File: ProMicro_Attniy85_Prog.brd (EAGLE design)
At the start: 31.7 x 21.6 mm, 10 parts, among them U1 ATTINY85-20P

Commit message: Add files via upload
Minor changes
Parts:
- moved R1 1.59 mm to (27.6, 8.89)
- moved R2 1.59 mm to (27.6, 11.4)
- moved R3 1.59 mm to (27.6, 14.0)
- moved LED3 1.31 mm to (23.2, 9.21)
- moved LED1 1.27 mm to (23.2, 14.0)
- moved LED2 1.27 mm to (23.2, 11.4)
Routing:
- net PIN9: track 32.5 -> 30.2 mm
- net PIN7: track 36.5 -> 37.2 mm
- net VCC: track 14.6 -> 14.0 mm

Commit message: Add files via upload
Minor changes
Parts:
- moved C1 0.95 mm to (17.5, 11.4)
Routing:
- net RST: track 11.7 -> 12.7 mm
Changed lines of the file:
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@@
 <wire x1="21.2725" y1="14.9225" x2="21.2725" y2="7.9375" width="0.2032" layer="21"/>
 <wire x1="21.2725" y1="7.9375" x2="24.765" y2="7.9375" width="0.2032" layer="21"/>
-<text x="17.145" y="9.525" size="0.8128" layer="21" rot="R90">10nF</text>
+<text x="16.1925" y="9.525" size="0.8128" layer="21" rot="R90">10nF</text>
 <text x="20.955" y="11.43" size="0.8128" layer="21" rot="R90" align="bottom-center">LED</text>
 <text x="29.845" y="7.62" size="0.8128" layer="21" align="top-right">220ohm</text>
@@
 <elements>
 <element name="U1" library="_hhn_attiny25_45_85 (1)" package="PDIP08_300MIL" value="ATTINY85-20P" x="8.89" y="11.43" smashed="yes" rot="R180"/>
-<element name="C1" library="rc-master-smd" package="C0805" value="" x="18.415" y="11.43" smashed="yes" rot="R270">
-<attribute name="NAME" x="19.685" y="13.208" size="0.8128" layer="25" ratio="18" rot="R270"/>
-<attribute name="VALUE" x="16.637" y="13.208" size="0.6096" layer="27" ratio="10" rot="R270"/>
+<element name="C1" library="rc-master-smd" package="C0805" value="" x="17.4625" y="11.43" smashed="yes" rot="R270">
+<attribute name="NAME" x="16.3195" y="13.6525" size="0.8128" layer="25" ratio="18"/>
+<attribute name="VALUE" x="15.6845" y="13.208" size="0.6096" layer="27" ratio="10" rot="R270"/>
 </element>
 <element name="JP2" library="pinhead" library_urn="urn:adsk.eagle:library:325" package="2X12" package3d_urn="urn:adsk.eagle:package:22420/2" value="" x="16.51" y="19.05" smashed="yes" rot="R180">
@@
 <wire x1="22.86" y1="20.32" x2="22.86" y2="17.78" width="0.4064" layer="1"/>
 <wire x1="25.4" y1="20.32" x2="25.4" y2="17.78" width="0.4064" layer="1"/>
-<wire x1="22.86" y1="17.78" x2="22.5425" y2="17.78" width="0.4064" layer="1"/>
-<wire x1="22.5425" y1="17.78" x2="18.415" y2="13.6525" width="0.4064" layer="1"/>
-<wire x1="18.415" y1="13.6525" x2="18.415" y2="13.716" width="0.4064" layer="1"/>
-<wire x1="18.415" y1="12.446" x2="18.415" y2="13.6525" width="0.4064" layer="1"/>
+<wire x1="17.4625" y1="12.446" x2="17.4625" y2="12.7635" width="0.4064" layer="1"/>
 <wire x1="5.08" y1="15.24" x2="7.874" y2="12.446" width="0.4064" layer="1"/>
-<wire x1="7.874" y1="12.446" x2="18.415" y2="12.446" width="0.4064" layer="1"/>
+<wire x1="7.874" y1="12.446" x2="17.4625" y2="12.446" width="0.4064" layer="1"/>
 <wire x1="22.86" y1="20.32" x2="25.4" y2="20.32" width="0.4064" layer="1"/>
 <via x="16.51" y="6.985" extent="1-16" drill="0.35"/>
@@
 <vertex x="0.3175" y="-0.635"/>
 </polygon>
+<wire x1="17.4625" y1="12.446" x2="22.7965" y2="17.78" width="0.4064" layer="1"/>
+<wire x1="22.7965" y1="17.78" x2="22.86" y2="17.78" width="0.4064" layer="1"/>
+<wire x1="22.86" y1="17.78" x2="22.1275" y2="13.97" width="0" layer="19" extent="1-1"/>
+<wire x1="16.51" y1="6.985" x2="17.4625" y2="12.446" width="0" layer="19" extent="1-1"/>
 </signal>
 <signal name="VCC">
@@
 <wire x1="23.8125" y1="6.6675" x2="22.225" y2="6.6675" width="0.2032" layer="1"/>
 <wire x1="22.225" y1="6.6675" x2="18.4785" y2="10.414" width="0.2032" layer="1"/>
-<wire x1="18.415" y1="10.414" x2="18.4785" y2="10.414" width="0.2032" layer="1"/>
+<wire x1="17.4625" y1="10.414" x2="18.4785" y2="10.414" width="0.2032" layer="1"/>
 <contactref element="JP3" pad="19"/>
 <contactref element="JP3" pad="20"/>

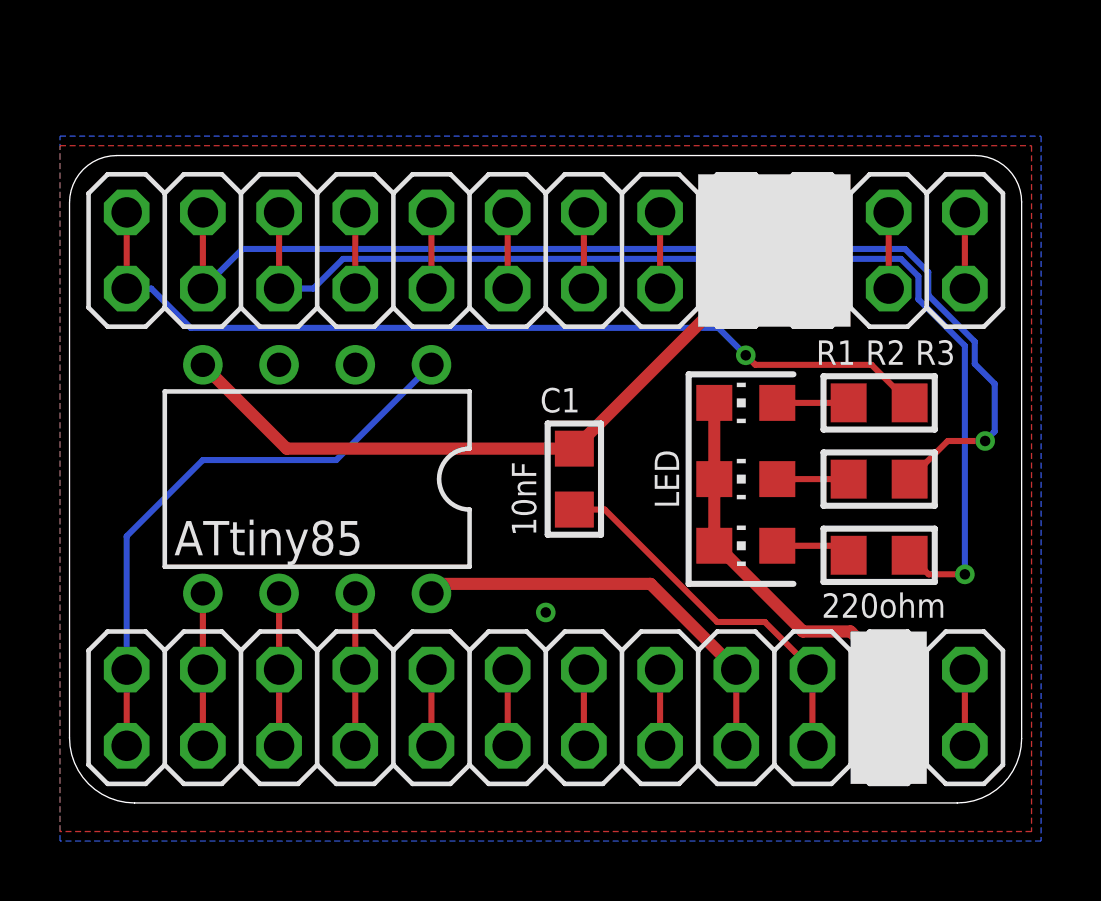
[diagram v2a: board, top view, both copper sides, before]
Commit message: Add files via upload
Wrong size, corrected... the old one only fits on the original pro micro with micro USB
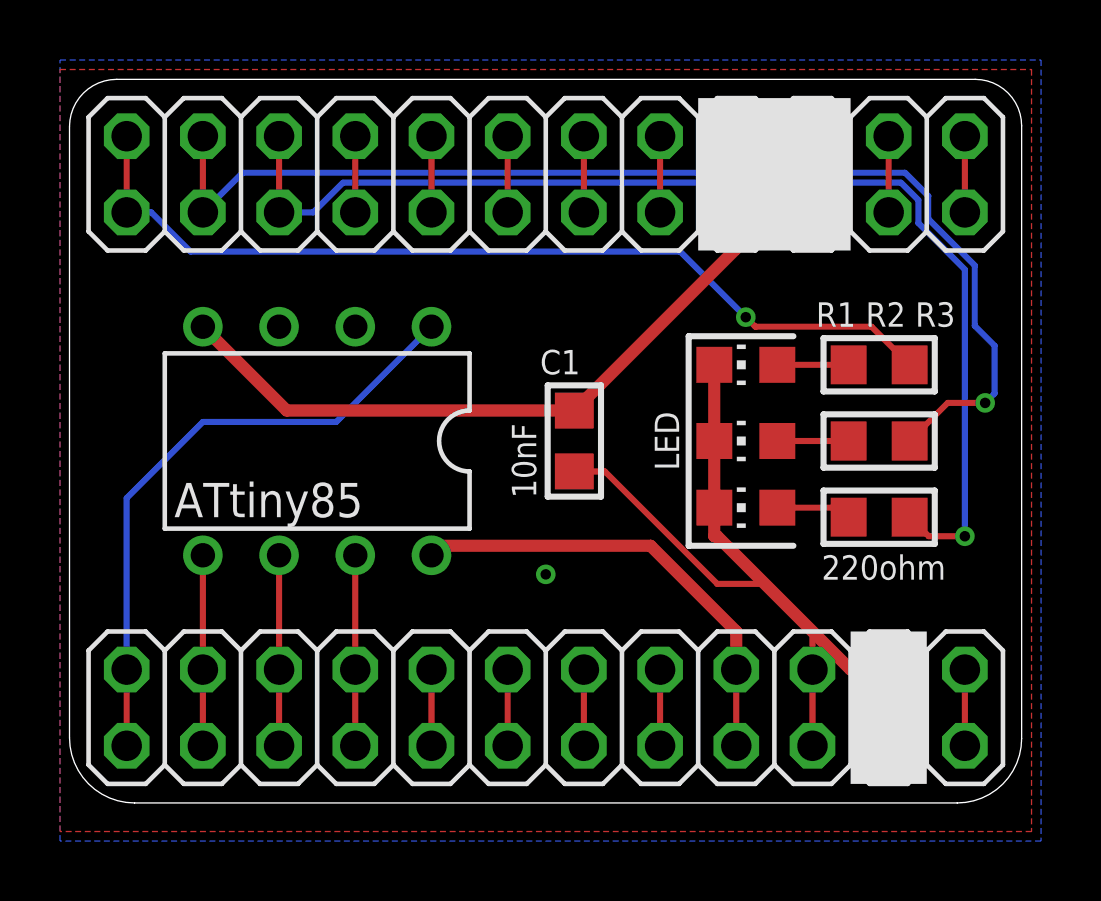
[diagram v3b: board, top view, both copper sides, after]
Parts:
- moved JP2 2.54 mm to (16.5, 21.6)
- moved C1 1.27 mm to (17.5, 12.7)
- moved LED1 1.27 mm to (23.2, 15.2)
- moved LED2 1.27 mm to (23.2, 12.7)
- moved LED3 1.27 mm to (23.2, 10.5)
- moved R1 1.27 mm to (27.6, 10.2)
- moved R2 1.27 mm to (27.6, 12.7)
- moved R3 1.27 mm to (27.6, 15.2)
- moved U1 1.27 mm to (8.89, 12.7)
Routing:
- net GND: track 43.9 -> 46.2 mm
- net PIN8: track 37.3 -> 38.6 mm
- net SCK: track 5.08 -> 6.35 mm
- net MOSI: track 5.08 -> 6.35 mm
- net MISO: track 5.08 -> 6.35 mm
- net VCC: track 14.0 -> 15.3 mm
- net RST: track 12.7 -> 14.0 mm
- net PIN7: track 37.2 -> 38.5 mm
- net PIN10: track 19.5 -> 20.8 mm
- net PIN9: track 30.2 -> 30.7 mm
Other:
- board size 31.7 x 21.6 mm -> 31.7 x 24.1 mm

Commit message: Add files via upload
As a recommendation from the AttinyCore85 Documentation, I've exchanged the capacitor (that was low) to an tantalum polar 100uf, and added another one of 0.1uf as coupler.
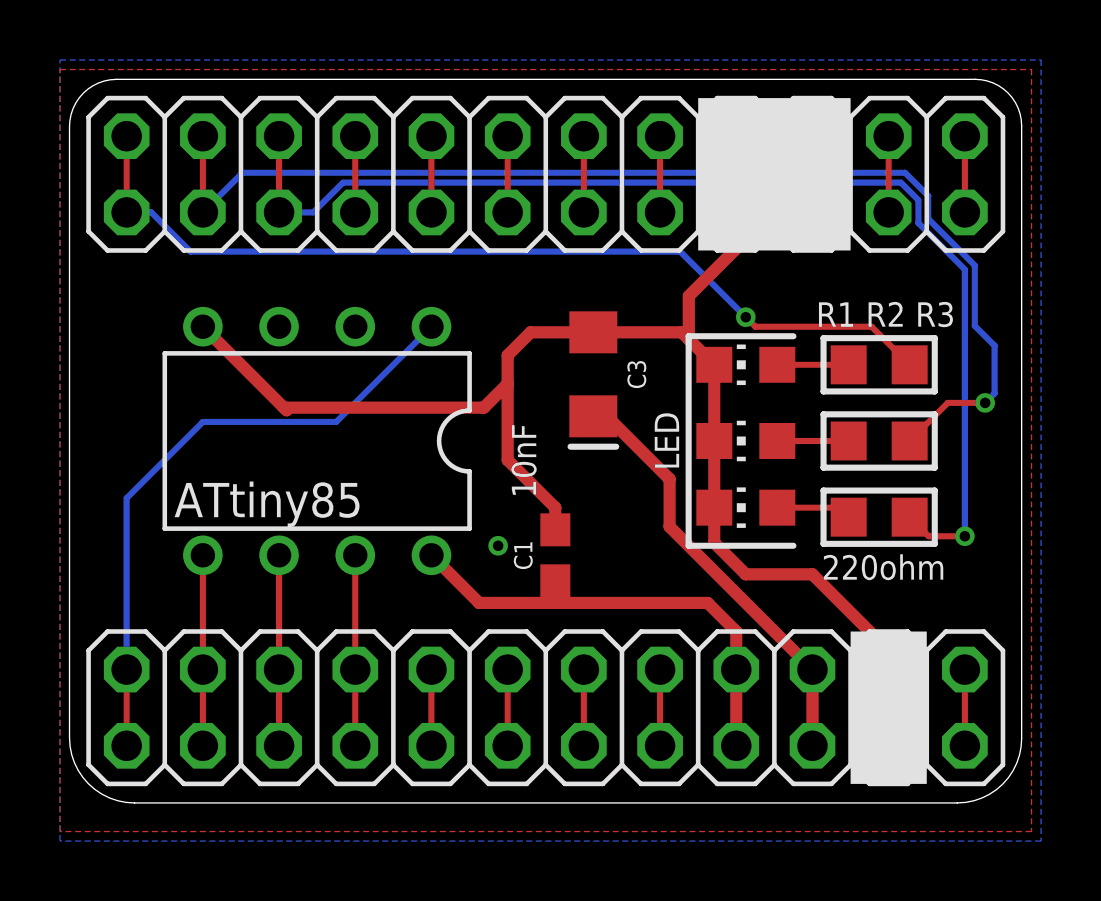
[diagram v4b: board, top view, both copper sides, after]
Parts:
- added C3: 10uF, SparkFun-Capacitors:EIA3216
- C1: value (none) -> 0.1uF; device rc-master-smd:C0805 -> SparkFun-Capacitors:0603
- moved C1 3.86 mm to (16.8, 8.89), turned to 90 degrees
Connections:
- net GND: now also C1.2, C3.-; no longer C1.1
- net RST: now also C3.+; no longer C1.2
- net VCC: now also C1.1
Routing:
- net GND: track 46.2 -> 54.8 mm
- net VCC: track 15.3 -> 15.9 mm
